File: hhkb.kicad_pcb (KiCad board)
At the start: 2 copper layers, 101.9 x 285.8 mm, 136 parts, among them J1 USB_mini_micro_B, SW1 SW_PUSH, U1 ATMEGA32U4, X1 XTAL_GND

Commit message: Done
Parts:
- removed D1:1: D, Diodes_SMD:D_SOD-123
- removed ESC1: KEYSW, TheKeebrary:MX_Plate_100H
- added HOLE_M3: VAL**, keyboard_parts:HOLE_M3, F.Cu at (0.00, 300.0)
- added HOLE_M3: VAL**, keyboard_parts:HOLE_M3, F.Cu at (266.7, 261.9)
- added HOLE_M3: VAL**, keyboard_parts:HOLE_M3, F.Cu at (173.8, 319.1)
- added HOLE_M3: VAL**, keyboard_parts:HOLE_M3, F.Cu at (59.5, 319.1)
- added HOLE_M3: VAL**, keyboard_parts:HOLE_M3, F.Cu at (64.3, 252.4)
- added HOLE_M3: VAL**, keyboard_parts:HOLE_M3, F.Cu at (157.2, 271.5)
- "'"1, ","1, "-"1, "."1, "/"1, "0"1, "1"1, "2"1, "3"1, "4"1, "5"1, "6"1, "7"1, "8"1, "9"1, ";"1, "="1, "A"1, "B"1, "C"1, "D"1, "E"1, "F"1, "G"1, "H"1, "I"1, "J"1, "K"1, "L"1, "M"1, "N"1, "O"1, "P"1, "Q"1, "R"1, "S"1, "T"1, "U"1, "V"1, "W"1, "X"1, "Y"1, "Z"1, "["1, "\"1, "]"1, "`"1, ALT1, R_ALT1, R_FN1: footprint TheKeebrary:MX_Plate_100H -> AlpsKeys:Alps100
- BS1, L_CMD1, R_CMD1: footprint TheKeebrary:MX_Plate_150H -> AlpsKeys:Alps150
- CTRL1: footprint TheKeebrary:MX_Plate_175H -> AlpsKeys:Alps100
- D10:10, D10:11, D10:12, D10:7, D10:8, D10:9, D1:3, D1:4, D1:5, D1:6, D2:1, D2:2, D2:3, D2:4, D2:5, D2:6, D3:1, D3:2, D3:3, D3:4, D3:5, D3:6, D4:1, D4:2, D4:3, D4:4, D4:5, D4:6, D5:1, D5:2, D5:3, D5:4, D5:5, D5:6, D6:12, D6:7, D6:8, D6:9, D7:10, D7:11, D7:12, D7:8, D7:9, D8:10, D8:11, D8:12, D8:7, D8:8, D8:9, D9:10, D9:11, D9:12, D9:7, D9:8, D9:9, D:6:10, D:6:11, D:7:7: footprint Diodes_SMD:D_SOD-123 -> Diodes_THT:D_T-1_P12.70mm_Horizontal; moved to F.Cu
- D1:2: footprint Diodes_SMD:D_SOD-123 -> Diodes_THT:D_T-1_P10.16mm_Horizontal; moved to F.Cu
- L_SHIFT1, RET1: footprint TheKeebrary:MX_Plate_225H -> AlpsKeys:Alps150
- R_SHIFT1: footprint TheKeebrary:MX_Plate_175H -> AlpsKeys:Alps150
- SPACEBAR1: footprint TheKeebrary:MX_Plate_600H_Stepped -> AlpsKeys:Alps600
- TAB1: footprint TheKeebrary:MX_Plate_150H -> AlpsKeys:Alps100
- moved D8:12 322.0 mm to (250.0, 288.1), turned to 90 degrees
- moved R_FN1 310.2 mm to (254.8, 300.0), turned to 0 degrees
- moved D6:12 308.9 mm to (250.0, 252.4)
- moved D7:12 305.0 mm to (237.6, 271.6)
- moved "`"1 303.9 mm to (259.6, 242.9), turned to 0 degrees
- moved BS1 297.7 mm to (254.8, 261.9), turned to 0 degrees
- moved D:6:11 293.9 mm to (250.0, 250.0), turned to 90 degrees
- moved D7:11 292.9 mm to (240.5, 269.1), turned to 90 degrees
- moved D8:11 292.2 mm to (226.2, 288.1), turned to 90 degrees
- moved RET1 286.6 mm to (240.5, 281.0), turned to 0 degrees
- moved "\"1 276.9 mm to (240.5, 242.9), turned to 0 degrees
- moved R_SHIFT1 275.6 mm to (231.0, 300.0), turned to 0 degrees
- moved D:6:10 267.0 mm to (231.0, 250.0), turned to 90 degrees
- moved D8:10 265.3 mm to (207.2, 288.1), turned to 90 degrees
- moved "]"1 264.1 mm to (231.0, 261.9), turned to 0 degrees
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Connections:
- J1 pad 4: Net-(J1-Pad4) -> (no net)
- U1 pad 1: Net-(U1-Pad1) -> (no net)
- U1 pad 11: /ROW5 -> /COL7
- U1 pad 12: /ROW4 -> /COL6
- U1 pad 18: Net-(U1-Pad18) -> /COL5
- U1 pad 19: Net-(U1-Pad19) -> /ROW6
- U1 pad 20: /COL4 -> /ROW7
- U1 pad 21: /COL5 -> /ROW8
- U1 pad 22: /COL6 -> /ROW1
- U1 pad 25: /ROW3 -> /COL11
- U1 pad 26: /ROW2 -> /COL8
- U1 pad 27: /ROW1 -> /ROW9
- U1 pad 28: /COL7 -> /ROW10
- U1 pad 29: /COL8 -> /COL10
- U1 pad 30: /ROW10 -> /COL9
- U1 pad 31: /COL9 -> /COL4
- U1 pad 32: /ROW9 -> /ROW2
- U1 pad 36: /COL10 -> (no net)
- U1 pad 37: /COL11 -> /ROW4
- U1 pad 38: /COL12 -> /ROW3
- U1 pad 39: /ROW8 -> /ROW5
- U1 pad 40: /ROW7 -> /COL1
- U1 pad 41: /ROW6 -> /COL2
- U1 pad 42: Net-(U1-Pad42) -> (no net)
- U1 pad 8: /COL1 -> /COL12
- U1 pad 9: /COL2 -> (no net)
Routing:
- net GND: track 916.3 -> 187.1 mm, vias 0 -> 14
- net Net-(J1-Pad2): track 514.1 -> 3.91 mm
- net Net-(J1-Pad3): track 510.5 -> 3.50 mm
- net VCC: track 588.4 -> 84.5 mm
- net /ROW9: track 83.2 -> 323.0 mm, vias 0 -> 2
- net /ROW10: track 36.3 -> 261.6 mm, vias 0 -> 2
- net /COL12: track 191.2 -> 387.4 mm
- net /COL11: track 214.0 -> 386.3 mm, vias 0 -> 5
- net /COL1: track 273.9 -> 104.6 mm, vias 0 -> 2
- net /COL9: track 149.2 -> 290.4 mm, vias 0 -> 4
- net /COL8: track 128.3 -> 267.7 mm, vias 0 -> 2
- net /COL3: track 295.8 -> 164.9 mm, vias 0 -> 5
- net /ROW5: track 127.0 -> 254.5 mm, vias 0 -> 2
- net /COL10: track 215.0 -> 334.0 mm, vias 0 -> 6
- net /ROW1: track 228.1 -> 127.9 mm, vias 0 -> 3
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- added copper zone on F.Cu, net GND
- added copper zone on B.Cu, net VCC
- removed copper zone on B.Cu, net GND
- removed copper zone on B.Cu, net Net-(J1-Pad6)
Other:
- board size 101.9 x 285.8 mm -> 276.2 x 101.2 mm

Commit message: Rm ground planes
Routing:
- net /COL11: track 386.3 -> 419.8 mm
- net /ROW8: track 242.5 -> 261.1 mm
- net /COL8: track 267.7 -> 282.9 mm
- net Net-("E"1-Pad2): track 7.46 -> 19.8 mm
- net /ROW10: track 261.6 -> 273.2 mm
- net Net-("["1-Pad2): track 7.46 -> 17.1 mm
- net /COL5: track 186.3 -> 176.8 mm
- net /ROW7: track 222.6 -> 231.4 mm
- net Net-(D9:12-Pad2): track 23.7 -> 15.2 mm
- net /COL3: track 164.9 -> 156.6 mm
- net /COL9: track 290.4 -> 282.6 mm
- net /ROW5: track 254.5 -> 247.1 mm
- net Net-(D5:3-Pad2): track 8.96 -> 16.2 mm
- net /COL2: track 186.9 -> 180.7 mm
- net Net-(CTRL1-Pad2): track 7.46 -> 11.8 mm
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
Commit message: Rotate 90 deg to print.
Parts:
- moved HOLE_M3 244.1 mm to (80.3, 104.3), turned to 90 degrees
- moved "`"1 237.9 mm to (61.2, 111.5), turned to 90 degrees
- moved R_FN1 228.9 mm to (118.4, 116.2), turned to 90 degrees
- moved BS1 227.4 mm to (80.3, 116.2), turned to 90 degrees
- moved D:6:11 222.8 mm to (68.4, 121.0), turned to 180 degrees
- moved D6:12 222.3 mm to (70.7, 121.0), turned to 90 degrees
- moved D8:12 220.3 mm to (106.5, 121.0), turned to 180 degrees
- moved D9:12 217.4 mm to (125.5, 125.8), turned to 180 degrees
- moved "\"1 211.6 mm to (61.2, 130.5), turned to 90 degrees
- moved D9:11 210.8 mm to (125.5, 130.5), turned to 180 degrees
- moved D7:11 206.5 mm to (87.4, 130.5), turned to 180 degrees
- moved RET1 206.3 mm to (99.3, 130.5), turned to 90 degrees
- moved D7:12 202.2 mm to (89.9, 133.4), turned to 90 degrees
- moved D:6:10 196.3 mm to (68.4, 140.0), turned to 180 degrees
- moved R_SHIFT1 195.7 mm to (118.4, 140.0), turned to 90 degrees
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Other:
- board size 276.2 x 101.2 mm -> 101.2 x 276.2 mm

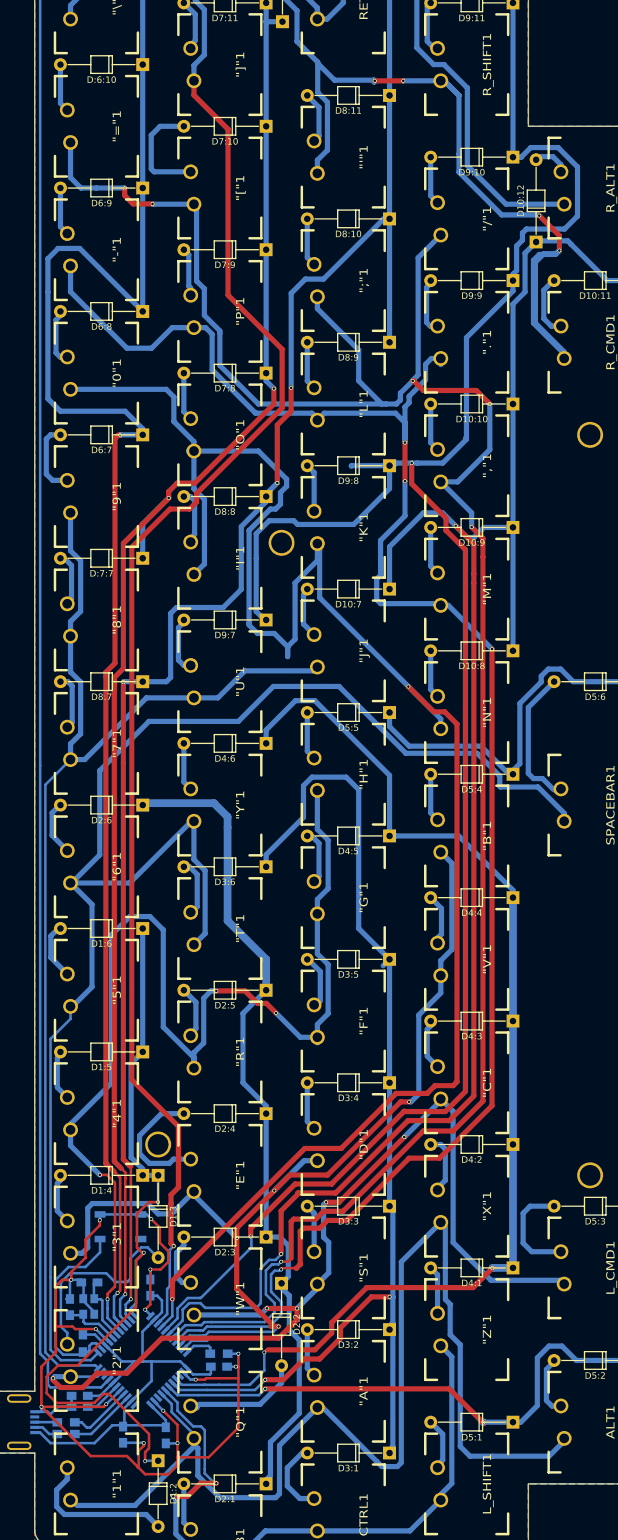
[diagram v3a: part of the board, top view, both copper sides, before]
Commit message: Via size to 0.8mm
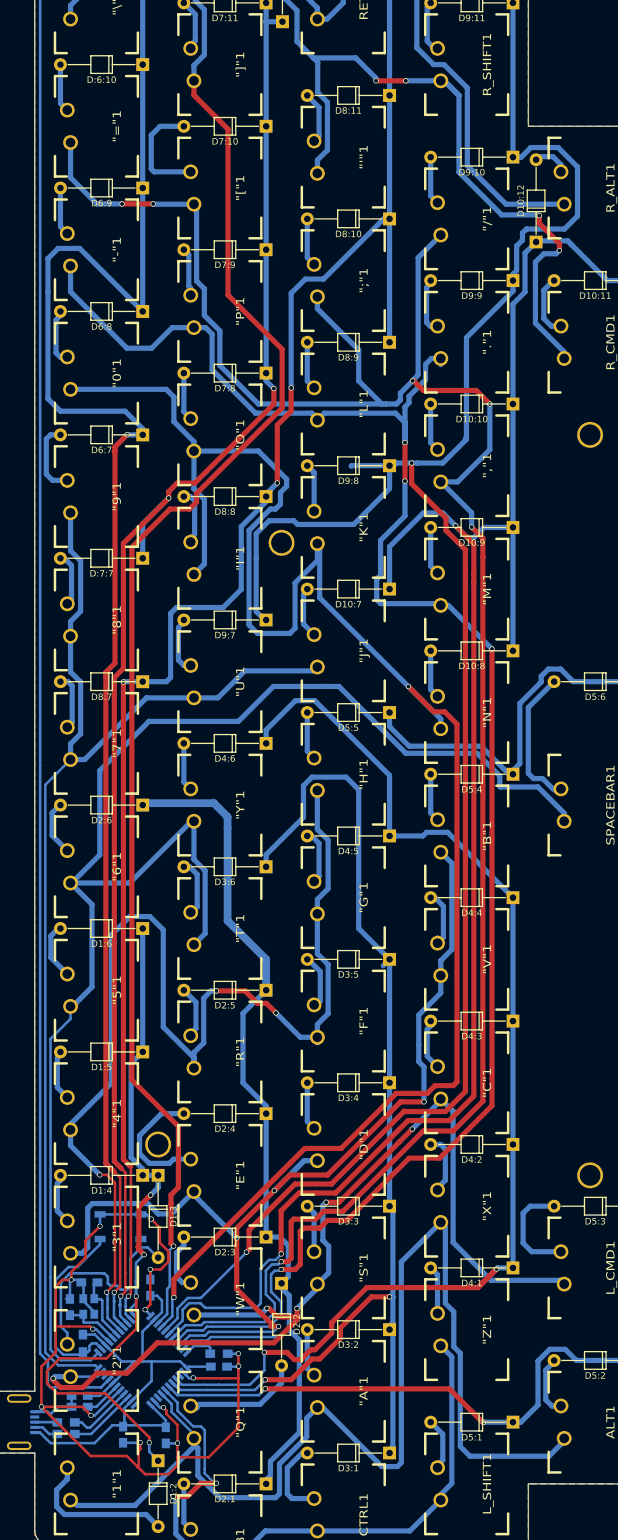
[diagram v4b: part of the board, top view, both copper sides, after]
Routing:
- net /COL11: track 419.8 -> 399.4 mm
- net /ROW1: track 123.9 -> 117.8 mm, vias 3 -> 4
- net /COL8: track 282.9 -> 277.1 mm
- net /ROW4: track 181.7 -> 186.5 mm
- net Net-("2"1-Pad2): track 31.5 -> 33.7 mm
- net /COL4: track 164.6 -> 166.4 mm
- net Net-("V"1-Pad2): track 7.96 -> 9.40 mm
- net VCC: track 84.5 -> 83.1 mm
- net GND: track 189.7 -> 191.0 mm
- net /ROW5: track 247.1 -> 246.3 mm
- net Net-(R1-Pad1): track 30.6 -> 29.9 mm
- net Net-(CTRL1-Pad2): track 11.8 -> 12.5 mm
- net /COL3: track 156.6 -> 157.2 mm
- net /ROW6: track 264.3 -> 263.8 mm
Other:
- net class Default: via_dia 0.6 -> 0.8; via_drill 0.4 -> 0.6
- rule via_min_drill: 0.3 -> 0.6
- rule via_min_size: 0.4 -> 0.8

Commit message: Reduce milling area
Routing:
- net Net-("D"1-Pad2): track 7.46 -> 13.8 mm
- net Net-(D5:3-Pad2): track 16.2 -> 21.5 mm
- net /COL9: track 282.6 -> 277.7 mm
- net /COL11: track 399.4 -> 395.4 mm
- net Net-("K"1-Pad2): track 7.46 -> 11.3 mm
- net Net-("="1-Pad2): track 7.46 -> 10.8 mm
- net /COL10: track 333.7 -> 335.9 mm
- net /ROW7: track 231.5 -> 233.5 mm
- net /ROW8: track 261.2 -> 263.0 mm
- net /COL5: track 177.0 -> 175.3 mm
- net /ROW6: track 263.8 -> 262.3 mm
- net /ROW3: track 173.2 -> 171.8 mm
- net Net-(ALT1-Pad2): track 9.35 -> 10.7 mm
- net Net-("Q"1-Pad2): track 20.1 -> 18.8 mm
- net Net-("L"1-Pad2): track 7.46 -> 8.52 mm
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
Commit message: Reduce milling area
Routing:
- net Net-("E"1-Pad2): track 19.8 -> 9.14 mm
- net /COL3: track 157.2 -> 155.5 mm
- net /COL4: track 166.4 -> 165.0 mm
- net Net-("X"1-Pad2): track 9.37 -> 8.41 mm
- net Net-("'"1-Pad2): track 8.09 -> 9.03 mm
- net /COL11: track 395.4 -> 394.7 mm

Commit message: Set via size ot 1mm
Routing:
- net /COL10: track 335.9 -> 327.6 mm
- net /ROW4: track 186.2 -> 192.2 mm, vias 2 -> 1
- net /ROW1: track 117.7 -> 115.2 mm
- net /COL9: track 277.7 -> 279.8 mm
- net /ROW3: track 171.5 -> 169.9 mm, vias 2 -> 1
- net /ROW6: track 262.6 -> 264.1 mm, vias 2 -> 1
- net /ROW9: track 320.2 -> 321.5 mm, vias 2 -> 1
- net /ROW10: track 273.2 -> 274.3 mm, vias 2 -> 1
- net Net-("["1-Pad2): track 16.2 -> 15.1 mm
- net GND: track 190.3 -> 191.3 mm, vias 14 -> 13
- net Net-("`"1-Pad2): track 16.9 -> 16.0 mm
- net /COL4: track 165.0 -> 164.0 mm
- net /COL8: track 277.5 -> 276.8 mm
- net /COL5: track 175.3 -> 176.0 mm
- net /COL3: track 155.5 -> 156.1 mm
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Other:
- net class Default: via_dia 0.8 -> 1
- rule via_min_size: 0.8 -> 1
